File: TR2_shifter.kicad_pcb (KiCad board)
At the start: 2 copper layers, 70 x 30 mm, 28 parts, among them U1 - LM339 LM339_DIP, U2 - LM339 LM339_DIP

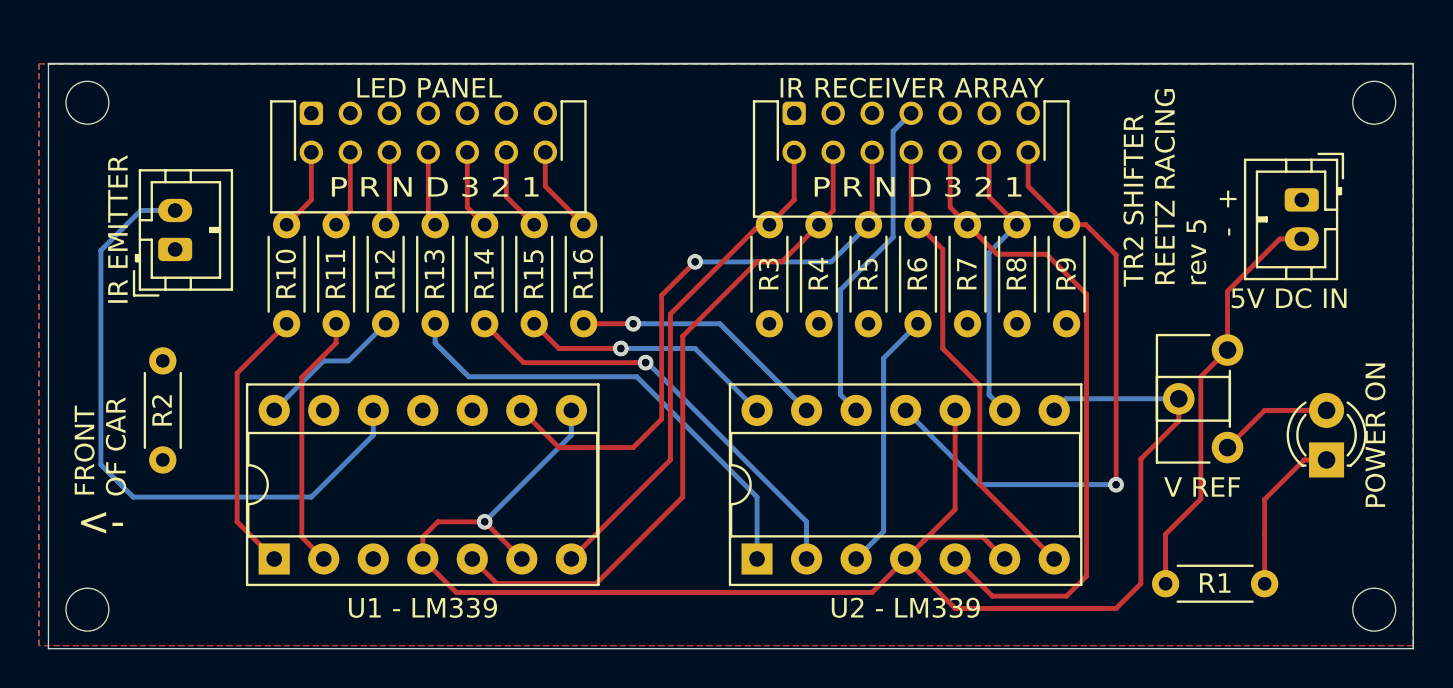
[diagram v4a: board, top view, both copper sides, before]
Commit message: Tweaking silkscreen, and adjust a zone so it fits within board dimensions
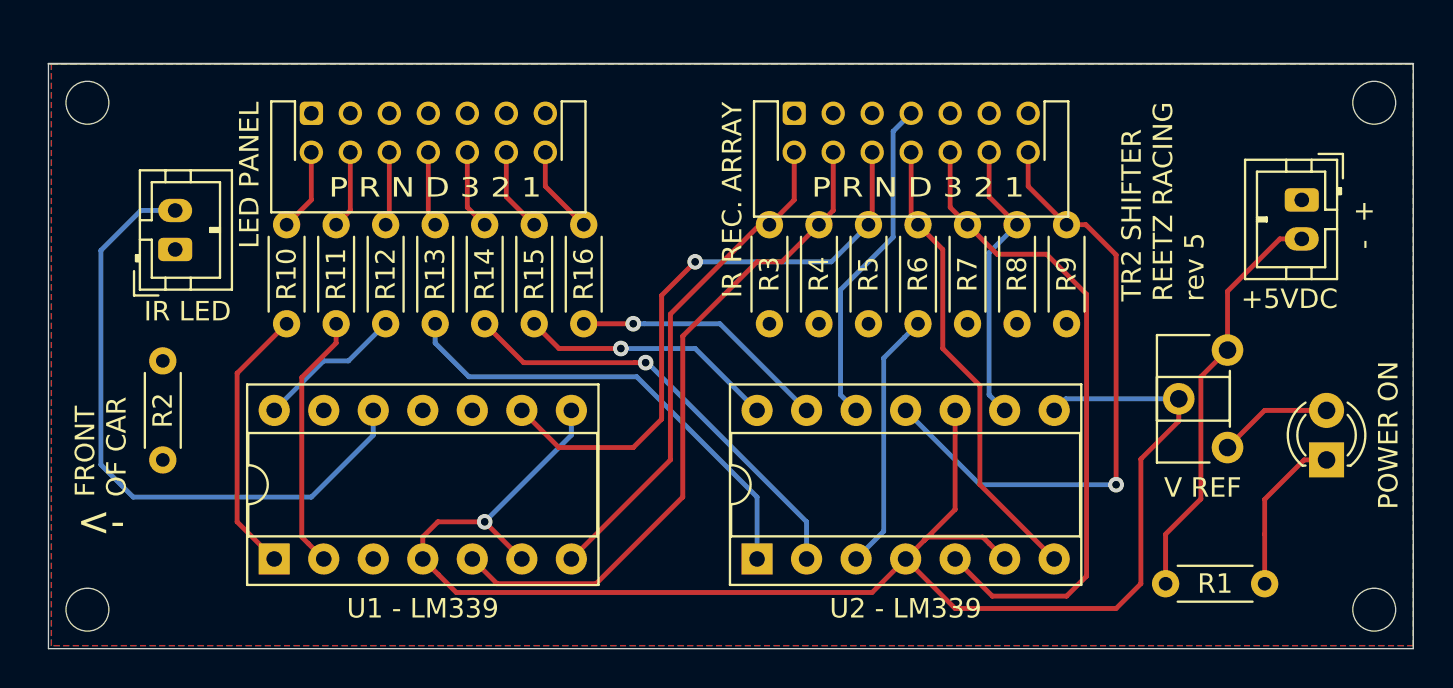
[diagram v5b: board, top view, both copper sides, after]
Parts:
- removed IR RECEIVER ARRAY: Conn_02x07_Odd_Even, Connector_JST:JST_PHD_S14B-PHDSS_2x07_P2.00mm_Horizontal
- added IR REC. ARRAY: Conn_02x07_Odd_Even, Connector_JST:JST_PHD_S14B-PHDSS_2x07_P2.00mm_Horizontal, F.Cu at (189.9, 71.1)
- +5VDC: renamed from 5V DC IN
- IR LED: renamed from IR EMITTER
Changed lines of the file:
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@@
     (38 B.Mask user)
     (39 F.Mask user)
-    (40 Dwgs.User user)
-    (41 Cmts.User user)
+    (40 Dwgs.User user hide)
+    (41 Cmts.User user hide)
     (42 Eco1.User user)
     (43 Eco2.User user)
     (44 Edge.Cuts user)
     (45 Margin user)
-    (46 B.CrtYd user)
-    (47 F.CrtYd user)
+    (46 B.CrtYd user hide)
+    (47 F.CrtYd user hide)
     (48 B.Fab user)
-    (49 F.Fab user)
+    (49 F.Fab user hide)
   )
   (setup
@@
     (descr "JST PHD series connector, S14B-PHDSS (http://www.jst-mfg.com/product/pdf/eng/ePHD.pdf), generated with kicad-footprint-generator")
     (tags "connector JST PHD horizontal")
-    (fp_text reference "LED PANEL" (at 6 -1.27) (layer F.SilkS)
-      (effects (font (size 1 1) (thickness 0.15)))
+    (fp_text reference "LED PANEL" (at -3.175 3.175 90) (layer F.SilkS)
+      (effects (font (size 1 1) (thickness 0.25)))
     )
     (fp_text value Conn_02x07_Odd_Even (at 6 11.43) (layer F.Fab)
@@
     (descr "JST PHD series connector, S14B-PHDSS (http://www.jst-mfg.com/product/pdf/eng/ePHD.pdf), generated with kicad-footprint-generator")
     (tags "connector JST PHD horizontal")
-    (fp_text reference "IR RECEIVER ARRAY" (at 6 -1.27) (layer F.SilkS)
-      (effects (font (size 1 1) (thickness 0.15)))
+    (fp_text reference "IR REC. ARRAY" (at -3.175 4.445 90) (layer F.SilkS)
+      (effects (font (size 1 1) (thickness 0.25)))
     )
     (fp_text value Conn_02x07_Odd_Even (at 6 10.2) (layer F.Fab)
@@
     (descr "LED, diameter 3.0mm, 2 pins")
     (tags "LED diameter 3.0mm 2 pins")
-    (fp_text reference "POWER ON" (at 1.27 2.54 90) (layer F.SilkS)
+    (fp_text reference "POWER ON" (at 1.27 3.175 90) (layer F.SilkS)
       (effects (font (size 1 1) (thickness 0.15)))
     )
@@
     (tags "THT DIP DIL PDIP 2.54mm 7.62mm 300mil Socket")
     (fp_text reference "U2 - LM339" (at -2.54 7.62 180) (layer F.SilkS)
-      (effects (font (size 1 1) (thickness 0.15)))
+      (effects (font (size 1 1) (thickness 0.25)))
     )
     (fp_text value LM339_DIP (at 3.81 17.57 90) (layer F.Fab)
@@
     (tags "THT DIP DIL PDIP 2.54mm 7.62mm 300mil Socket")
     (fp_text reference "U1 - LM339" (at -2.54 7.62 180) (layer F.SilkS)
-      (effects (font (size 1 1) (thickness 0.15)))
+      (effects (font (size 1 1) (thickness 0.25)))
     )
     (fp_text value LM339_DIP (at 3.81 17.57 90) (layer F.Fab)
@@
     (descr "JST PH series connector, B2B-PH-K (http://www.jst-mfg.com/product/pdf/eng/ePH.pdf), generated with kicad-footprint-generator")
     (tags "connector JST PH side entry")
-    (fp_text reference "IR EMITTER" (at 1 -2.9 90) (layer F.SilkS)
+    (fp_text reference "IR LED" (at -3.175 0.635 180) (layer F.SilkS)
       (effects (font (size 1 1) (thickness 0.15)))
     )
@@
     (descr "JST PH series connector, B2B-PH-K (http://www.jst-mfg.com/product/pdf/eng/ePH.pdf), generated with kicad-footprint-generator")
     (tags "connector JST PH side entry")
-    (fp_text reference "5V DC IN" (at 5.08 0.635 180) (layer F.SilkS)
+    (fp_text reference +5VDC (at 5.08 0.635 180) (layer F.SilkS)
       (effects (font (size 1 1) (thickness 0.15)))
     )
@@
     (effects (font (size 1.5 1.5) (thickness 0.3)) (justify mirror))
   )
-  (gr_text "+  -" (at 212.09 76.2 90) (layer F.SilkS)
+  (gr_text "+  -" (at 219.075 76.835 90) (layer F.SilkS)
     (effects (font (size 1 1) (thickness 0.25)) (justify mirror))
   )
@@
     (effects (font (size 1 1.2) (thickness 0.15)))
   )
-  (gr_text "TR2 SHIFTER\nREETZ RACING\nrev 5" (at 208.915 80.01 90) (layer F.SilkS)
+  (gr_text "TR2 SHIFTER\nREETZ RACING\nrev 5" (at 208.788 80.772 90) (layer F.SilkS)
     (effects (font (size 1 1) (thickness 0.25)) (justify left))
   )
@@
     (polygon
       (pts
-        (xy 221.615 98.425) (xy 151.13 98.425) (xy 151.13 68.58) (xy 221.615 68.58)
+        (xy 221.615 98.425) (xy 151.765 98.425) (xy 151.765 68.58) (xy 221.615 68.58)
       )
     )
@@
     (polygon
       (pts
-        (xy 221.615 98.425) (xy 151.13 98.425) (xy 151.13 68.58) (xy 221.615 68.58)
+        (xy 221.615 98.425) (xy 151.765 98.425) (xy 151.765 68.58) (xy 221.615 68.58)
       )
     )

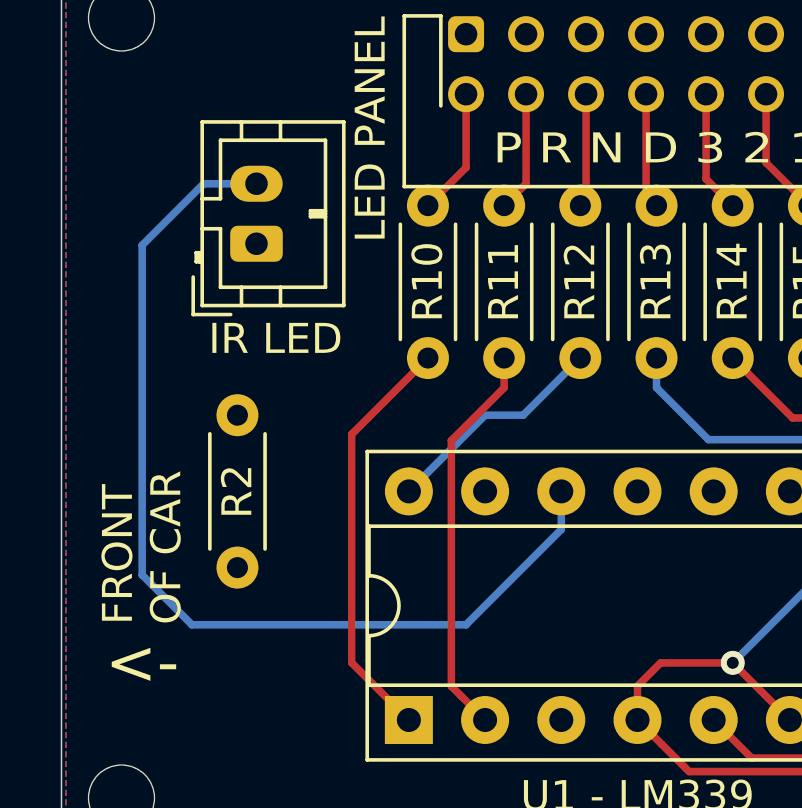
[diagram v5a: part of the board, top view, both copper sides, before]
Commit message: Fixed an error in emitter wiring
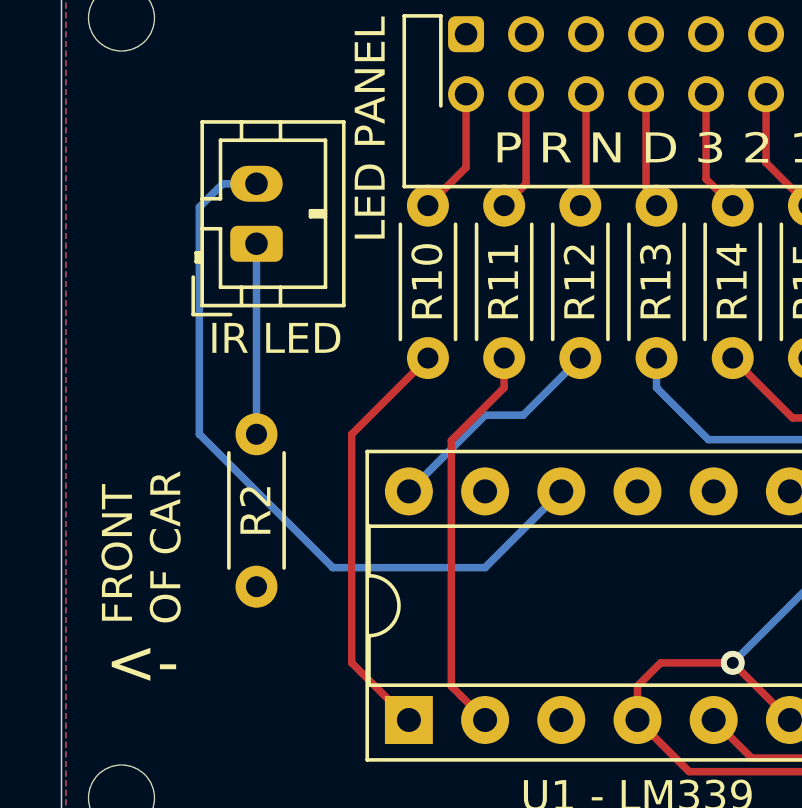
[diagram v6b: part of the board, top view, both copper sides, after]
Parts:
- moved R2 5.75 mm to (158.1, 89.5), turned to 90 degrees
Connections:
- IR LED pad 1: +5V -> Net-(J3-Pad1)
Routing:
- net GND: track 71.2 -> 63.1 mm
- net Net-(J3-Pad1): track 0.00 -> 6.35 mm
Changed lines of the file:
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@@
     (38 B.Mask user)
     (39 F.Mask user)
-    (40 Dwgs.User user hide)
-    (41 Cmts.User user hide)
+    (40 Dwgs.User user)
+    (41 Cmts.User user)
     (42 Eco1.User user)
     (43 Eco2.User user)
     (44 Edge.Cuts user)
     (45 Margin user)
-    (46 B.CrtYd user hide)
-    (47 F.CrtYd user hide)
+    (46 B.CrtYd user)
+    (47 F.CrtYd user)
     (48 B.Fab user)
-    (49 F.Fab user hide)
+    (49 F.Fab user)
   )
   (setup
@@
     (pad 2 thru_hole oval (at 2 0 90) (size 1.2 1.75) (drill 0.75) (layers *.Cu *.Mask)
       (net 1 GND))
-    (pad 1 thru_hole roundrect (at 0 0 90) (size 1.2 1.75) (drill 0.75) (layers *.Cu *.Mask) (roundrect_rratio 0.208333)
-      (net 7 +5V))
+    (pad 1 thru_hole roundrect (at 0 0 90) (size 1.2 1.75) (drill 0.75) (layers *.Cu *.Mask) (roundrect_rratio 0.208)
+      (net 20 "Net-(J3-Pad1)"))
     (model ${KISYS3DMOD}/Connector_JST.3dshapes/JST_PH_B2B-PH-K_1x02_P2.00mm_Vertical.wrl
       (at (xyz 0 0 0))
@@
   )
   (module Resistor_THT:R_Axial_DIN0204_L3.6mm_D1.6mm_P5.08mm_Horizontal (layer F.Cu)
-    (at 157.48 83.82 270)
+    (at 158.115 89.535 90)
     (descr "Resistor, Axial_DIN0204 series, Axial, Horizontal, pin pitch=5.08mm, 0.167W, length*diameter=3.6*1.6mm^2, http://cdn-reichelt.de/documents/datenblatt/B400/1_4W%23YAG.pdf")
     (tags "Resistor Axial_DIN0204 series Axial Horizontal pin pitch 5.08mm 0.167W length 3.6mm diameter 1.6mm")
@@
     (fp_line (start 0.74 0.8) (end 4.34 0.8) (layer F.Fab) (width 0.1))
     (fp_line (start 0.74 -0.8) (end 0.74 0.8) (layer F.Fab) (width 0.1))
-    (pad 2 thru_hole oval (at 5.08 0 270) (size 1.4 1.4) (drill 0.7) (layers *.Cu *.Mask)
+    (pad 2 thru_hole oval (at 5.08 0 90) (size 1.4 1.4) (drill 0.7) (layers *.Cu *.Mask)
       (net 20 "Net-(J3-Pad1)"))
-    (pad 1 thru_hole circle (at 0 0 270) (size 1.4 1.4) (drill 0.7) (layers *.Cu *.Mask)
+    (pad 1 thru_hole circle (at 0 0 90) (size 1.4 1.4) (drill 0.7) (layers *.Cu *.Mask)
       (net 7 +5V))
     (model ${KISYS3DMOD}/Resistor_THT.3dshapes/R_Axial_DIN0204_L3.6mm_D1.6mm_P5.08mm_Horizontal.wrl
@@
   (segment (start 210.725001 84.629999) (end 210.725001 90.899999) (width 0.25) (layer F.Cu) (net 1))
   (segment (start 212.09 83.265) (end 210.725001 84.629999) (width 0.25) (layer F.Cu) (net 1))
-  (segment (start 154.305 89.147002) (end 155.962998 90.805) (width 0.25) (layer B.Cu) (net 1))
-  (segment (start 154.305 78.155) (end 154.305 89.147002) (width 0.25) (layer B.Cu) (net 1))
-  (segment (start 155.962998 90.805) (end 165.1 90.805) (width 0.25) (layer B.Cu) (net 1))
-  (segment (start 168.275 87.63) (end 168.275 86.36) (width 0.25) (layer B.Cu) (net 1))
-  (segment (start 165.1 90.805) (end 168.275 87.63) (width 0.25) (layer B.Cu) (net 1))
   (segment (start 194.939999 72.045001) (end 194.939999 77.475001) (width 0.25) (layer B.Cu) (net 1))
   (segment (start 195.865 71.12) (end 194.939999 72.045001) (width 0.25) (layer B.Cu) (net 1))
@@
   (segment (start 192.240001 85.560001) (end 193.04 86.36) (width 0.25) (layer B.Cu) (net 1))
   (segment (start 194.939999 77.475001) (end 192.240001 80.174999) (width 0.25) (layer B.Cu) (net 1))
-  (segment (start 156.355 76.105) (end 158.115 76.105) (width 0.25) (layer B.Cu) (net 1))
-  (segment (start 154.305 78.155) (end 156.355 76.105) (width 0.25) (layer B.Cu) (net 1))
+  (segment (start 165.735 88.9) (end 168.275 86.36) (width 0.25) (layer B.Cu) (net 1))
+  (segment (start 160.655 88.9) (end 165.735 88.9) (width 0.25) (layer B.Cu) (net 1))
+  (segment (start 156.21 76.885) (end 156.21 84.455) (width 0.25) (layer B.Cu) (net 1))
+  (segment (start 156.99 76.105) (end 156.21 76.885) (width 0.25) (layer B.Cu) (net 1))
+  (segment (start 156.21 84.455) (end 160.655 88.9) (width 0.25) (layer B.Cu) (net 1))
+  (segment (start 158.115 76.105) (end 156.99 76.105) (width 0.25) (layer B.Cu) (net 1))
   (segment (start 189.865 75.565) (end 188.595 76.835) (width 0.25) (layer F.Cu) (net 2))
   (segment (start 189.865 73.12) (end 189.865 75.565) (width 0.25) (layer F.Cu) (net 2))
@@
   (via (at 173.99 92.075) (size 0.8) (drill 0.4) (layers F.Cu B.Cu) (net 19))
   (segment (start 178.435 87.63) (end 173.99 92.075) (width 0.25) (layer B.Cu) (net 19))
+  (segment (start 158.115 78.105) (end 158.115 84.455) (width 0.25) (layer B.Cu) (net 20))
   (segment (start 213.995 92.71) (end 213.995 95.25) (width 0.25) (layer F.Cu) (net 21))
   (segment (start 213.995 90.925) (end 213.995 92.71) (width 0.25) (layer F.Cu) (net 21))

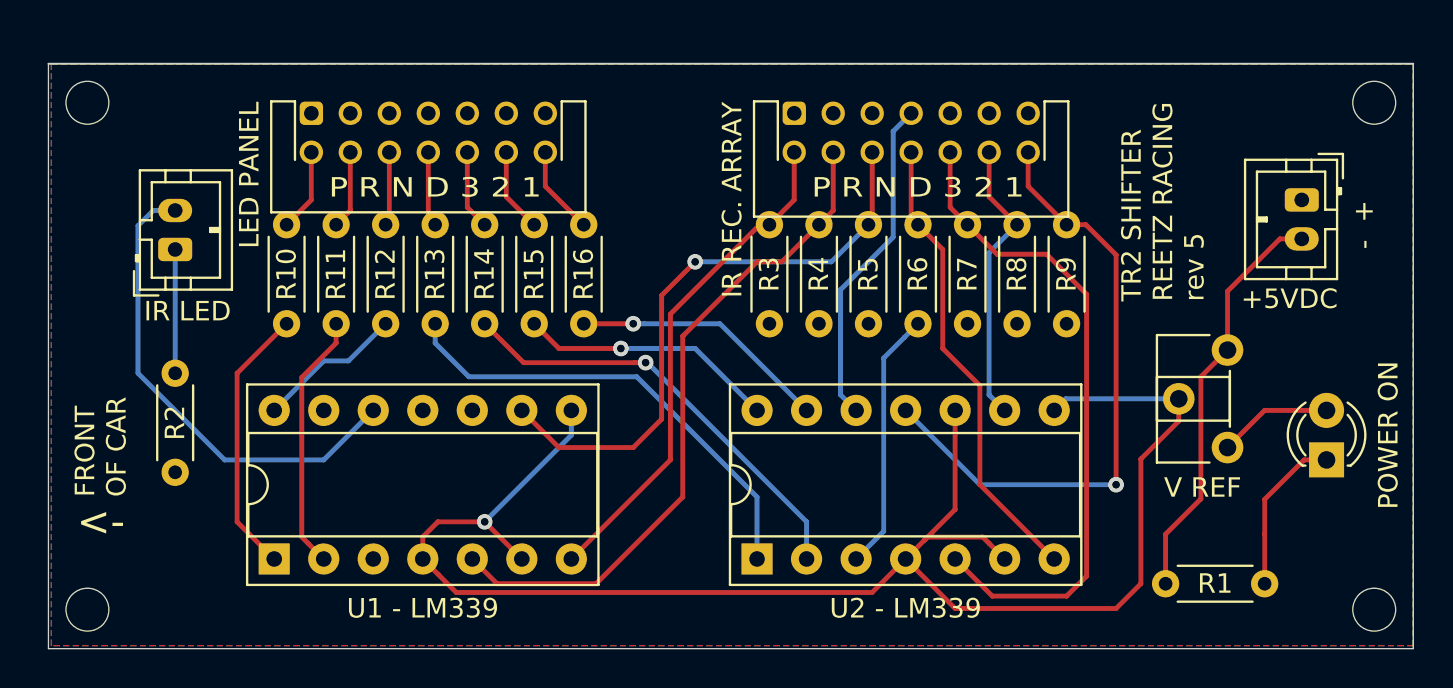
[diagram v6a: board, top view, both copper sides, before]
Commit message: Add connector polarity to silk
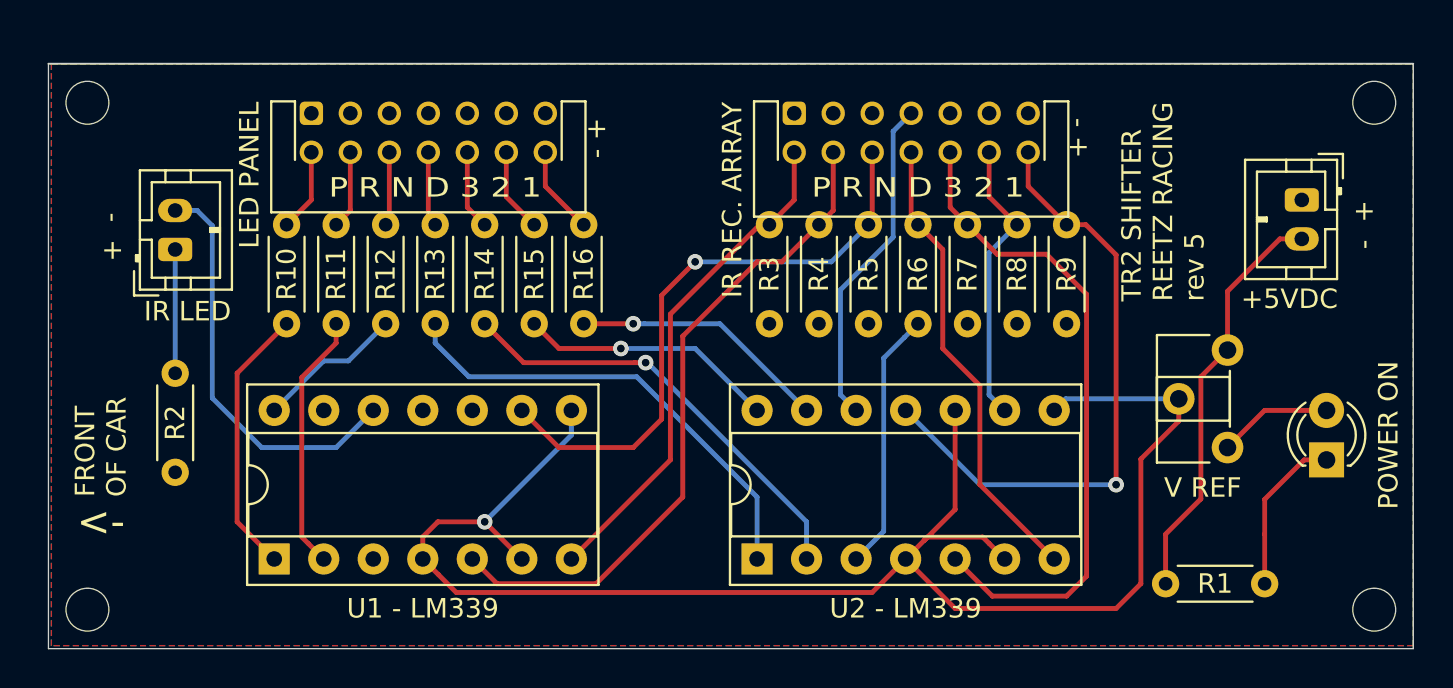
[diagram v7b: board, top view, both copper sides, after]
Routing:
- net GND: track 63.1 -> 59.5 mm
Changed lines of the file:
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@@
   (general
     (thickness 1.6)
-    (drawings 10)
+    (drawings 13)
     (tracks 158)
     (zones 0)
@@
     )
   )
+  (gr_text "+ -" (at 204.47 72.39 270) (layer F.SilkS)
+    (effects (font (size 1 1) (thickness 0.25)) (justify mirror))
+  )
+  (gr_text "+ -" (at 179.705 72.39 90) (layer F.SilkS)
+    (effects (font (size 1 1) (thickness 0.25)) (justify mirror))
+  )
+  (gr_text "+  -" (at 154.94 77.47 270) (layer F.SilkS)
+    (effects (font (size 1 1) (thickness 0.25)) (justify mirror))
+  )
   (gr_line (start 221.615 98.58) (end 221.615 68.58) (layer Edge.Cuts) (width 0.05))
   (gr_line (start 151.615 98.58) (end 221.615 98.58) (layer Edge.Cuts) (width 0.05))
@@
   (segment (start 192.240001 85.560001) (end 193.04 86.36) (width 0.25) (layer B.Cu) (net 1))
   (segment (start 194.939999 77.475001) (end 192.240001 80.174999) (width 0.25) (layer B.Cu) (net 1))
-  (segment (start 165.735 88.9) (end 168.275 86.36) (width 0.25) (layer B.Cu) (net 1))
-  (segment (start 160.655 88.9) (end 165.735 88.9) (width 0.25) (layer B.Cu) (net 1))
-  (segment (start 156.21 76.885) (end 156.21 84.455) (width 0.25) (layer B.Cu) (net 1))
-  (segment (start 156.99 76.105) (end 156.21 76.885) (width 0.25) (layer B.Cu) (net 1))
-  (segment (start 156.21 84.455) (end 160.655 88.9) (width 0.25) (layer B.Cu) (net 1))
-  (segment (start 158.115 76.105) (end 156.99 76.105) (width 0.25) (layer B.Cu) (net 1))
+  (segment (start 159.24 76.105) (end 160.02 76.885) (width 0.25) (layer B.Cu) (net 1))
+  (segment (start 158.115 76.105) (end 159.24 76.105) (width 0.25) (layer B.Cu) (net 1))
+  (segment (start 160.02 76.885) (end 160.02 85.725) (width 0.25) (layer B.Cu) (net 1))
+  (segment (start 162.56 88.265) (end 166.37 88.265) (width 0.25) (layer B.Cu) (net 1))
+  (segment (start 160.02 85.725) (end 162.56 88.265) (width 0.25) (layer B.Cu) (net 1))
+  (segment (start 166.37 88.265) (end 168.275 86.36) (width 0.25) (layer B.Cu) (net 1))
   (segment (start 189.865 75.565) (end 188.595 76.835) (width 0.25) (layer F.Cu) (net 2))
   (segment (start 189.865 73.12) (end 189.865 75.565) (width 0.25) (layer F.Cu) (net 2))
